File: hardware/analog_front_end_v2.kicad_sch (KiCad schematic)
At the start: 105 parts, among them J1 Conn_Coaxial, J3 Conn_01x01_Socket, J4 Conn_01x01_Socket, U1 ADL5531, U10 MAX6002, U11 LP2985-5.0, U12 MAX2606, U13 PAT1220-C-0DB, U14 LP2985-5.0, U15 BFP540ESD, U16 BFP540ESD, U17 LP2985-3.3, U18 PAT1220-C-0DB, U19 PAT1220-C-0DB, U2 ADL5531, U20 PAT1220-C-0DB, U21 PAT1220-C-0DB, U22 MCP6286, U3 ADL5531, U4 ADL5531, U5 LP2985-1.8, U6 MCP33131, U7 PAT1220-C-0DB, U8 ADL5531, U9 PMOD 2x6 2.54mm pitch

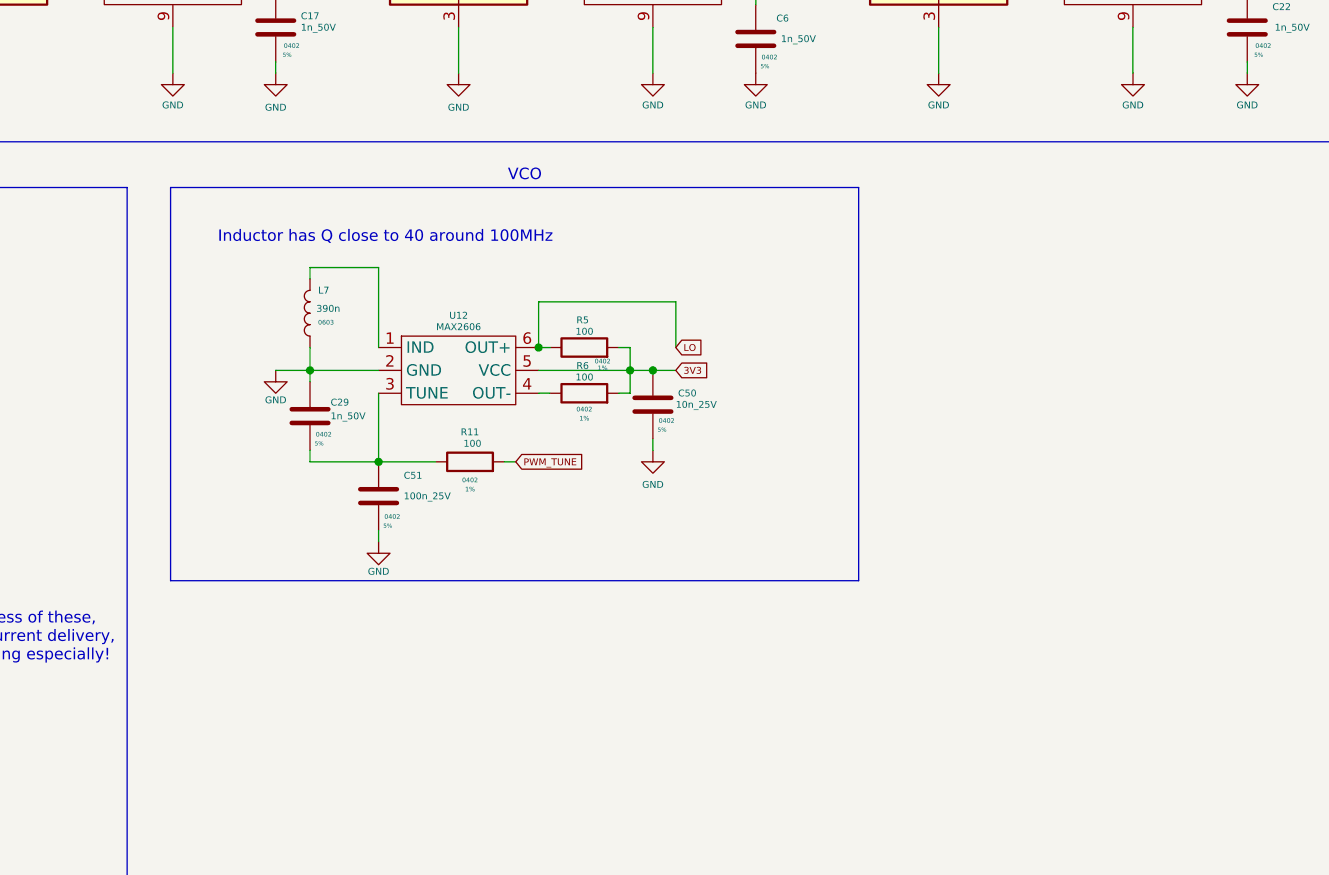
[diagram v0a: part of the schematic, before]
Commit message: Remove old VCO and start adding new one
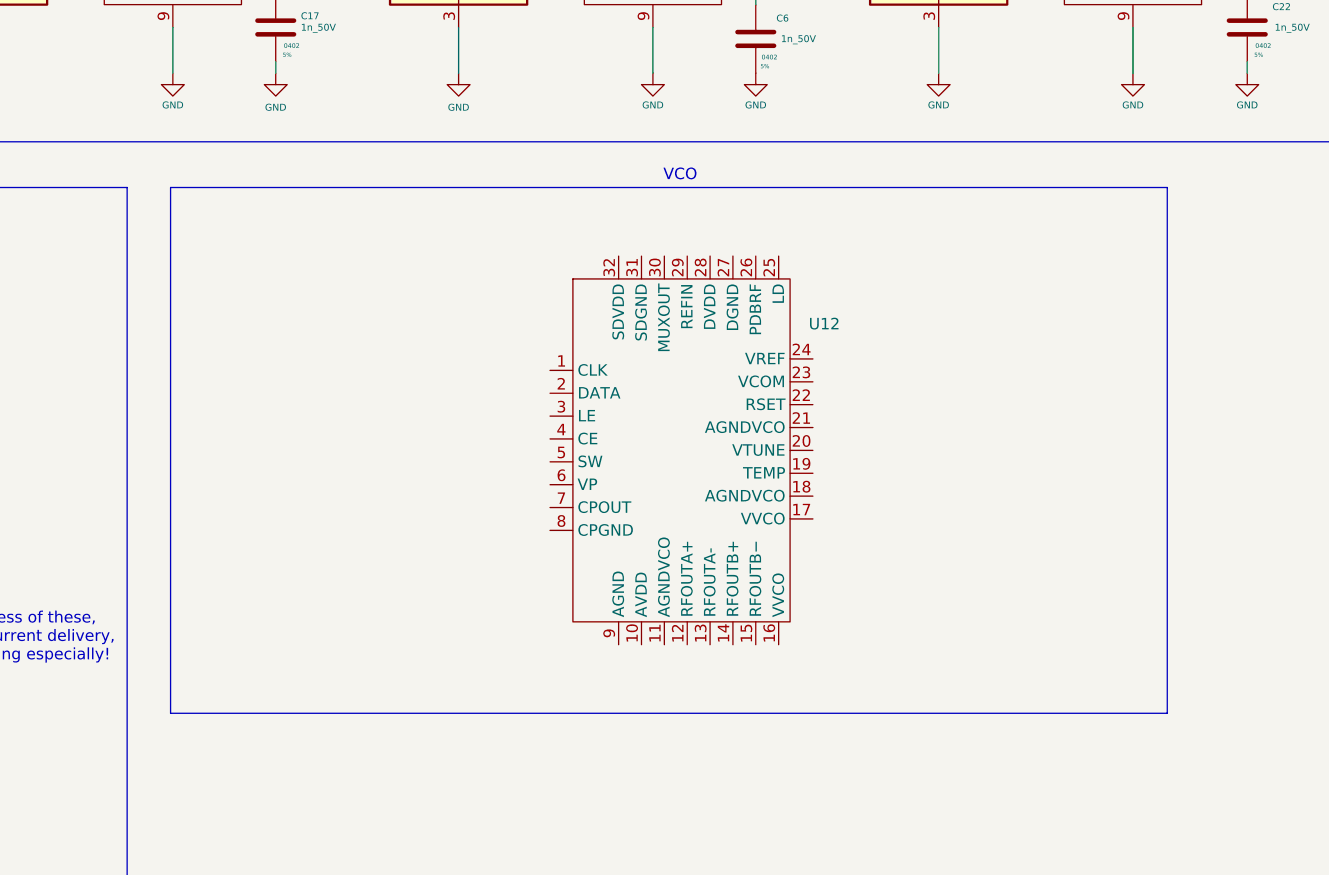
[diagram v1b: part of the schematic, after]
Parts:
- removed C29: 1n_50V, Capacitor_SMD:C_0402_1005Metric, symbol Device:C
- removed C50: 10n_25V, Capacitor_SMD:C_0402_1005Metric, symbol Device:C
- removed C51: 100n_25V, Capacitor_SMD:C_0402_1005Metric, symbol Device:C
- removed L7: 390n, Inductor_SMD:L_0603_1608Metric, symbol Device:L
- removed R11, R5, R6: 100, Resistor_SMD:R_0402_1005Metric, symbol Device:R
- removed U12: MAX2606, Package_TO_SOT_SMD:SOT-23-6, symbol TheEEView_Global_Lib:MAX2606
- added U12: (no value), symbol fmradio:ADF4351
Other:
- note removed: "Inductor has Q close to 40 around 100MHz"

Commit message: Beginnings of new VCO schem
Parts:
- added C55, C56, C57, C58: 100n_25V, Capacitor_SMD:C_0402_1005Metric, symbol Device:C
- added R11: 5.1k, Resistor_SMD:R_0402_1005Metric, symbol Device:R
- U12: value (none) -> ADF4531
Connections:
- net 3V3: now also U12.10 (AVDD), U12.17 (VVCO), U12.32 (SDVDD), U12.4 (CE), U12.6 (VP), C55.1, C56.1, C57.1, C58.1
- net GND: now also U12.11 (AGNDVCO), U12.18 (AGNDVCO), U12.27 (DGND), U12.31 (SDGND), U12.8 (CPGND), U12.9 (AGND), C55.2, C56.2, C57.2, C58.2, R11.2
- net at U12.22 (RSET): now also R11.1

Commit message: Schematic cleanups/working on new VCO connections
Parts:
- added U23: PMOD 2x6 2.54mm pitch, Connector_PinHeader_2.54mm:PinHeader_2x06_P2.54mm_Vertical, symbol TheEEView_Global_Lib:PMOD_2x6
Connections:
- net 3.3V_PMOD: now also U23.12, U23.6
- net ADC_SDO: now also U23.7
- net GND: now also U23.11, U23.5
- net VCO_SCLK: now reaches U12.1 (CLK)
- net VCO_SCLK: now also U23.3
- net VCO_DATA: now reaches U12.2 (DATA)
- net VCO_DATA: now also U23.1
- net VCO_LE: now reaches U12.3 (LE)
- net VCO_LE: now also U23.9
- net VCO_LOCKDET: now reaches U12.30 (MUXOUT)
- net VCO_LOCKDET: now also U23.10
- net PWM_TUNE: no longer names the net of U9.10
- no-connect marks 28 -> 31
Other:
- note added: "Arty S7 JA Connector"
- note added: "Arty S7 JB Connector"
- note added: "TODO: Draw footprint"
- note removed: "Arty S7 Connector"
- moved on the sheet: C1, C10, C11, C12, C13, C14, C15, C16, C17, C18, C19, C2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

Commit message: Add symbol for ADF4351 and update bandpass to 100 to 106MHz
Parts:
- removed C34, C35, C37, C39: 5p1_50V, Capacitor_SMD:C_0402_1005Metric, symbol Device:C
- removed L13: 100n, Inductor_SMD:L_0402_1005Metric, symbol Device:L
- removed R10, R8, R9: 3.3k, Resistor_SMD:R_0402_1005Metric, symbol Device:R
- removed U15, U16: BFP540ESD, Package_TO_SOT_SMD:SOT-343_SC-70-4_Handsoldering, symbol TheEEView_Global_Lib:BFP540ESD
- added U24: LT5560, Package_DFN_QFN:DFN-8-1EP_3x3mm_P0.5mm_EP1.66x2.38mm, symbol RF_Mixer:LT5560
- C2, C4: value 5p1_50V -> 4p8_50V; MOC GCM1555C1H5R1FA16D -> GJM1555C1H4R8BB01D
- C3: value 240p_50V -> 220p_50V; MOC GRT1555C1H241FA02D -> GRT1555C1H221FA02D
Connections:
- net 3V3: now also U12.28 (DVDD)
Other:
- note added: "100 - 106 MHz : 2nd order LC passive RF Band Pass Filter"
- note added: "EN > 2V for ON"
- note added: "Mix down to baseband for ADC sampling"
- note added: "NB: Intentionally leave SW o.c."
- note added: "TODO: Change to 100MHz to 106MHz"
- note added: "TODO: Change to an LT5560"
- note added: "TODO: Recheck if this gain amount is correct for the new downmixer and ADC"
- note added: "The LT5560 is characterized and production tested with a single-ended LO drive"
- note removed: "88 - 108 MHz : 2nd order LC passive RF Band Pass Filter"
- note removed: "Cascode based mixer for 86MHz to 106MHz band"
- moved on the sheet: C26, C27, C28, C52, C53, C54, L6, R2, R3, U10, U22, U23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

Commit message: Remove bandpass TODO
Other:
- note removed: "TODO: Change to 100MHz to 106MHz"
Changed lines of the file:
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@@
-		)
-	)
-	(text "TODO: Change to 100MHz to 106MHz"
-		(exclude_from_sim no)
-		(at 43.18 41.656 0)
-		(effects
-			(font
-				(size 1.27 1.27)
-			)
 		)
 	)

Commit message: Populate VCO and add butterworth filter immediately after before the ADC
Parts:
- removed C22: 1n_50V, Capacitor_SMD:C_0402_1005Metric, symbol Device:C
- removed C23, C24, C53: 10n_25V, Capacitor_SMD:C_0402_1005Metric, symbol Device:C
- removed C25, C26: 1u_16V, Capacitor_SMD:C_0603_1608Metric, symbol Device:C
- removed L12: 470n, Inductor_SMD:L_1008_2520Metric, symbol Device:L
- removed L6: 10n, Inductor_SMD:L_0805_2012Metric, symbol Device:L
- removed R3: 100, Resistor_SMD:R_0402_1005Metric, symbol Device:R
- removed U13: PAT1220-C-0DB, RF_Converter:RF_Attenuator_Susumu_PAT1220, symbol RF:PAT1220-C-0DB
- removed U8: ADL5531, TheEEView_Footprint_Lib:ADL5531, symbol TheEEView_Global_Lib:ADL5531
- added C59: 27p, Capacitor_SMD:C_0402_1005Metric, symbol Device:C
- added C60, C64, C67: 1n, Capacitor_SMD:C_0402_1005Metric, symbol Device:C
- added C61, C62, C84: 10n, Capacitor_SMD:C_0402_1005Metric, symbol Device:C
- added C63: 100p, Capacitor_SMD:C_0402_1005Metric, symbol Device:C
- added C65, C66, C68, C80, C82, C86: 100n, Capacitor_SMD:C_0402_1005Metric, symbol Device:C
- added C69, C78, C79, C81, C83: 1u, Capacitor_SMD:C_0402_1005Metric, symbol Device:C
- added C70: 390p, Capacitor_SMD:C_0402_1005Metric, symbol Device:C
- added C71, C72: 130p, Capacitor_SMD:C_0402_1005Metric, symbol Device:C
- added C73: 910p, Capacitor_SMD:C_0402_1005Metric, symbol Device:C
- added C74, C75: 56p, Capacitor_SMD:C_0402_1005Metric, symbol Device:C
- added C76, C77: 1n8, Capacitor_SMD:C_0402_1005Metric, symbol Device:C
- added C85: 10u, Capacitor_SMD:C_0402_1005Metric, symbol Device:C
- added FB1: 600R@100M, Inductor_SMD:L_0402_1005Metric, symbol Device:FerriteBead
- added L13, L14: 18n, Inductor_SMD:L_0402_1005Metric, symbol Device:L
- added R31: 3R0, Resistor_SMD:R_0402_1005Metric, symbol Device:R
- added R32: 162R, Resistor_SMD:R_0402_1005Metric, symbol Device:R
- added R33, R34: 330R, Resistor_SMD:R_0402_1005Metric, symbol Device:R
- added R35, R36, R37, R38, R41, R42, R43, R44: 1k00, Resistor_SMD:R_0402_1005Metric, symbol Device:R
- added R39, R40, R45, R46: 4k02, Resistor_SMD:R_0402_1005Metric, symbol Device:R
- added R47, R48: 22R0, Resistor_SMD:R_0402_1005Metric, symbol Device:R
- added R49, R50: 20k0, Resistor_SMD:R_0402_1005Metric, symbol Device:R
- added R51, R52: 50R, Resistor_SMD:R_0402_1005Metric, symbol Device:R
- added T1: WBC1-1TL 1:1, symbol Device:Transformer_1P_SS
- added U15: LP2985-5.0, Package_TO_SOT_SMD:SOT-23-5, symbol Regulator_Linear:LP2985-5.0
- added U25, U26: LTC6362, Package_DFN_QFN:DFN-8-1EP_3x3mm_P0.5mm_EP1.66x2.38mm, symbol Amplifier_Operational:LTC6362xDD
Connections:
- net 3V3: now also U12.16 (VVCO), U12.26 (PDBRF), R51.1, R52.2
- net ADC_VREF_2V5: now also R49.1
- net GND: now also U12.21 (AGNDVCO), U24.9 (PGND), C60.2, C61.2, C67.2, C68.2, C69.2, C76.1, C77.2, C78.2, C79.2, C80.2, C81.2, C82.2, C83.2, C84.2, C85.1, C86.1, R31.2, R32.2, R50.2, T1.2 (AB), U15.2 (GND), U25.6 (V-), U25.9 (V-), U26.6 (V-), U26.9 (V-); no longer U6.4 (AIN-)
- net VIN: now also U15.1 (VIN), U15.3 (ON/~{OFF})
- net VCM_DIV: now reaches U22.3 (Vin+)
- net VCM_DIV: now also C78.1, R49.2, R50.1
- net LO_100M: now reaches U12.12 (RFOUTA+)
- net LO_100M: now also C63.1, R51.2
- net at U12.13 (RFOUTA-): now also R52.1
- net ADC_AIN_P: now reaches U6.3 (AIN+)
- net ADC_AIN_P: now also C76.2, R47.2
- net at U24.1 (LO-): now also C62.2
- net 5V_MIX: now reaches U24.2 (EN)
- net 5V_MIX: now also U24.7 (VCC), C67.1, C68.1, C69.1, C80.1, C81.1, C82.1, C83.1, FB1.2, R33.1, R34.2, U25.3 (V+), U25.7 (~{SHDN}), U26.3 (V+), U26.7 (~{SHDN})
- net at U24.3 (IN+): now also L13.2
- net at U24.4 (IN-): now also L14.2
- net at U24.5 (OUT-): now also C64.2, C66.1, R34.1
- net at U24.6 (OUT+): now also C64.1, C65.1, R33.2
- net at U24.8 (LO+): now also C61.1
- net at U7.2: now also T1.1 (AA)
- net ADC_VCM: now reaches R2.2
- net ADC_VCM: now also C79.1, U25.2 (VOCM), U26.2 (VOCM)
- new net: C62.1, C63.2, R32.1
- new net: C85.2, C86.2, FB1.1, U15.5 (VOUT)
- new net: C70.2, R36.2, R38.1, R40.1
- new net: C72.2, R40.2, R42.1, U25.5 (-)
- new net: C59.2, L14.1, T1.3 (SA)
- new net: C73.2, R42.2, R44.1, R46.1
- new net: C72.1, R38.2, U25.8 (+)
- new net: C71.2, R39.2, R41.1, U25.4 (+)
- new net: C73.1, R41.2, R43.1, R45.1
- new net: C70.1, R35.2, R37.1, R39.1
- new net: C71.1, R37.2, U25.1 (-)
- new net: C84.1, U15.4 (BP)
- new net: C59.1, L13.1, T1.5 (SB)
- new net: C75.1, R44.2, U26.8 (+)
- new net: C75.2, R46.2, R48.1, U26.5 (-)
- new net: C74.1, R43.2, U26.1 (-)
- new net: C74.2, R45.2, R47.1, U26.4 (+)
- new net ADC_AIN_N: C77.1, R48.2, U6.4 (AIN-)
- new net IF_N: C66.2, R36.1
- new net IF_P: C65.2, R35.1
- new net MIX_BIAS: C60.1, R31.1, T1.4 (SC)
- no-connect marks 31 -> 26
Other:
- note added: "22R / 1n8 charge kickback (DS20005947C Fig 6-2)"
- note added: "4th-order Butterworth MFB, fc 249 kHz, differential gain 16.2"
- note added: "4x20dB fixed gain LNA's (80dB total gain)"
- note added: "ADC common mode, 1.25 V"
- note added: "Anti-aliasing now at U25/U26 (4th order, 249kHz)"
- note added: "LT5560 downmixer: 100 MHz RF, LO one IF low, 100 kHz IF"
- note added: "Q = 0.54"
- note added: "Q = 1.27"
- note added: "R31 sets I_CC = 10 mA; C60 for noise figure"
- note added: "RFOUTA+ to mixer LO; A- terminated"
- note added: "V_CM buffer: VREF/2 = 1.25V"
- note added: "V_CM buffered by U22 (MCP6286)"
- note removed: "320kHz anti-aliasing filter"
- note removed: "5x20dB fixed gain LNA's (100dB total gain)"
- note removed: "DC shift for ADC"
- note removed: "TODO: Change to an LT5560"
- moved on the sheet: C27, C28, C30, C31, C32, C33, C36, C38, C40, C41, C42, C43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

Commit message: Populate remainder of schematic
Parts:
- added C87, C92, C93, C94: 100n, Capacitor_SMD:C_0402_1005Metric, symbol Device:C
- added C88: 1u, Capacitor_SMD:C_0402_1005Metric, symbol Device:C
- added C89: 1n5, Capacitor_SMD:C_0402_1005Metric, symbol Device:C
- added C90: 15n, Capacitor_SMD:C_0402_1005Metric, symbol Device:C
- added C91: 150p, Capacitor_SMD:C_0402_1005Metric, symbol Device:C
- added R53: 33R, Resistor_SMD:R_0402_1005Metric, symbol Device:R
- added R54: 1k37, Resistor_SMD:R_0402_1005Metric, symbol Device:R
- added R55: 6k19, Resistor_SMD:R_0402_1005Metric, symbol Device:R
- added TP23: LOCK_DET, TestPoint:TestPoint_Pad_D1.0mm, symbol Connector:TestPoint
- added Y1: 12.8MHz TCXO, Oscillator:Oscillator_SMD_Abracon_ASE-4Pin_3.2x2.5mm, symbol Oscillator:ASE-xxxMHz
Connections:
- net 3V3: now also C87.1, C88.1, Y1.1 (EN), Y1.4 (Vdd)
- net GND: now also C87.2, C88.2, C89.2, C90.2, C91.2, C92.2, C93.2, C94.2, Y1.2 (GND)
- net PLL_TEMP: now reaches U12.19 (TEMP)
- net PLL_TEMP: now also C94.1
- net VTUNE: now reaches U12.20 (VTUNE)
- net VTUNE: now also C91.1, R55.2
- net PLL_VCOM: now reaches U12.23 (VCOM)
- net PLL_VCOM: now also C93.1
- net PLL_VREF: now reaches U12.24 (VREF)
- net PLL_VREF: now also C92.1
- net at U12.25 (LD): now also TP23.1
- net PLL_REF: now reaches U12.29 (REFIN)
- net PLL_REF: now also R53.2
- net CP_OUT: now reaches U12.7 (CPOUT)
- net CP_OUT: now also C89.1, R54.1, R55.1
- new net: R53.1, Y1.3 (OUT)
- new net: C90.1, R54.2
- no-connect marks 26 -> 29
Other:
- note added: "12.8 MHz TCXO -> PFD 3.2 MHz with R = 4"
- note added: "ADF4351 internal node decoupling"
- note added: "PLL loop filter: 19.8 kHz, 48 deg PM (I_CP 2.5 mA, K_V 40 MHz/V, N 1025)"
- moved on the sheet: C30, C31, C32, C33, C36, C38, C40, C41, C42, C43, C44, C45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

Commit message: Use 2nd 5V LNA for the 3rd and 4th amps
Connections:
- net 5V_LNA1: no longer C19.1, C20.1, L10.2
- net 5V_LNA2: now also C19.1, C20.1, L10.2
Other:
- moved on the sheet: C30, C31, C32, C33, C36, C38, C40, C41, C42, C43, C44, C45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
